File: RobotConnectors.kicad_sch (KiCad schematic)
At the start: 68 parts, among them J1 Conn_02x11_Top_Bottom, J10 Conn_01x05, J11 Conn_01x03_Male, J12 Conn_01x03_Male, J13 Conn_01x03_Male, J14 Conn_01x03_Male, J17 Conn_01x02, J18 Conn_01x02, J19 Conn_01x04, J2 Conn_02x04_Top_Bottom, J21 Conn_01x05, J27 Conn_01x03_Male, J28 Conn_01x03_Male, J29 Conn_01x03_Male, J3 Conn_01x02, J30 Conn_01x03_Male, J4 Conn_01x04, J5 Conn_01x04, J6 Conn_01x04, J7 Conn_01x04, J8 Conn_01x04, J9 Conn_01x04, U11 TXS0108EPW, U12 TXS0108EPW, U14 Fuse Holder, U15 Fuse Holder, U16 Fuse Holder, U17 Fuse Holder, U2 TPS2065CDBV, U28 Fuse 2A, U29 Fuse 2A

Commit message: Add Robot-Adapter and OEM plugs WIP
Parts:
- removed J11, J27, J28, J29, J30: Conn_01x03_Male, Connector_JST:JST_XH_B3B-XH-A_1x03_P2.50mm_Vertical, symbol Connector:Conn_01x03_Male
- removed J5, J6, J7, J8, J9: Conn_01x04, Connector_JST:JST_XH_B4B-XH-A_1x04_P2.50mm_Vertical, symbol Connector_Generic:Conn_01x04
- removed U11, U12: TXS0108EPW, Package_SO:TSSOP-20_4.4x6.5mm_P0.65mm, symbol Logic_LevelTranslator:TXS0108EPW
- added C62: 4.7uF, Capacitor_SMD:C_0805_2012Metric, symbol Device:C
- added C77: 100nF@50V, Capacitor_SMD:C_0402_1005Metric, symbol Device:C
- added J11: SA/SC Perimeter Plug, nlbn:ZX-HY2_0-9PZZ_C7429585, symbol Connector:Conn_01x09_Pin
- added J15: Hall0 (Stop2), Connector_JST:JST_XH_B3B-XH-A_1x03_P2.50mm_Vertical, symbol Connector:Conn_01x03_Male
- added J27: Rear Stop Switch 2, nlbn:HC-HY-2A_C2845460, symbol Connector:Conn_01x02_Pin
- added J40: Rear Stop Switch 1, nlbn:HC-HY-2A_C2845460, symbol Connector:Conn_01x02_Pin
- added J5: OEM CoverUI, nlbn:HDR-IDC-2_54-2X8P_C3406, symbol Connector_Generic:Conn_02x08_Odd_Even
- added J6: Conn_01x11_Socket, Connector_PinSocket_2.54mm:PinSocket_1x13_P2.54mm_Vertical, symbol Connector:Conn_01x13_Socket
- added J7: USS 1-5, Connector_PinSocket_2.54mm:PinSocket_1x12_P2.54mm_Vertical, symbol Connector:Conn_01x12_Socket
- added J8: Hall5 (Lift Left 2), Connector_JST:JST_XH_B3B-XH-A_1x03_P2.50mm_Vertical, symbol Connector:Conn_01x03_Male
- added J9: Hall4 (Lift Right 2), Connector_JST:JST_XH_B3B-XH-A_1x03_P2.50mm_Vertical, symbol Connector:Conn_01x03_Male
- added R28, R29, R30, R31, R32, R36, R37, R38, R39, R40, R42, R43, R60, R65: 10k, Resistor_SMD:R_0402_1005Metric, symbol Device:R
- added TP2: Hall6 (unused), TestPoint:TestPoint_Pad_D1.5mm, symbol Connector:TestPoint
- added U11, U12: SN74LVC07ADBR, nlbn:SN74LVC07ADBR_C2676799, symbol nlbn:SN74LVC07ADBR_C2676799
- added U47, U48: SN74LVC157ADR, PCM_JLCPCB:SOIC-16_3.9x9.9mm_P1.27mm, symbol 74xx:74LS157
- J12: value Conn_01x03_Male -> Hall3 (Lift Left)
- J13: value Conn_01x03_Male -> Hall2 (Lift Right)
- J14: value Conn_01x03_Male -> Hall1 (Stop1)
- R61, R62, R63, R64: now fitted
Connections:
- net 3.3V: now also C20.2, R48.1, R49.1, R50.1, C77.1, R28.1, R29.1, R60.1, R65.1, U11.14 (VCC), U12.14 (VCC), U47.16 (VCC), U48.16 (VCC); no longer R62.1
- net 5V: now also R62.1, C62.1, J15.1 (Pin_1), J5.9 (Pin_9), J6.1 (Pin_1), J7.1 (Pin_1), J8.1 (Pin_1), J9.1 (Pin_1), R30.1, R31.1, R32.1, R36.1, R37.1, R38.1, R39.1, R40.1, R42.1, R43.1; no longer C20.1, R48.1, R49.1, R50.1
- net GND: now also C20.1, C62.2, C77.2, J11.8 (Pin_8), J15.3 (Pin_3), J27.2 (Pin_2), J5.13 (Pin_13), J5.7 (Pin_7), J5.8 (Pin_8), J6.13 (Pin_13), J7.12 (Pin_12), J8.3 (Pin_3), J9.3 (Pin_3), U11.13 (6A), U11.7 (GND), U12.13 (6A), U12.7 (GND), U47.15 (E), U47.8 (GND), U48.15 (E), U48.2 (I0a), U48.3 (I1a), U48.8 (GND); no longer C20.2
- net HALL0: now also U47.12 (Zd); no longer R61.2
- net HALL0_5V: now also J15.2 (Pin_2), R40.2, U47.14 (I0d); no longer R51.2
- net HALL1: now also U47.9 (Zc); no longer R62.2
- net HALL1_5V: now also J14.2 (Pin_2), R39.2, U47.11 (I0c); no longer R50.2
- net HALL2: now also U47.7 (Zb); no longer R63.2
- net HALL2_5V: now also R38.2, U47.5 (I0b); no longer J14.2 (Pin_2), R49.2
- net HALL3: now also U47.4 (Za); no longer R64.2
- net HALL3_5V: now also R51.2, U47.2 (I0a); no longer R48.2
- net LED_RX: now also J5.3 (Pin_3)
- net LED_TX: now also J5.1 (Pin_1)
- net RAIN_SENSE: now also J5.11 (Pin_11)
- net USS1_ECHO: now also R28.2, U12.2 (1Y)
- net USS1_TRIGGER: now also U11.1 (1A)
- net USS2_ECHO: now also R29.2, U12.4 (2Y)
- net USS2_TRIGGER: now also U11.3 (2A)
- net USS3_ECHO: now also R48.2, U12.6 (3Y)
- net USS3_TRIGGER: now also U11.5 (3A)
- net USS4_ECHO: now also R50.2, U12.8 (4Y)
- net USS4_TRIGGER: now also U11.9 (4A)
- net USS5_ECHO: now also R49.2, U12.10 (5Y)
- net USS5_TRIGGER: now also U11.11 (5A)
- net USS_1_ECHO_5V: now also J7.11 (Pin_11), U12.1 (1A)
- net USS_1_TRIGGER_5V: now also J7.10 (Pin_10), R30.2, U11.2 (1Y)
- net USS_2_ECHO_5V: now also J7.9 (Pin_9), U12.3 (2A)
- net USS_2_TRIGGER_5V: now also J7.8 (Pin_8), R31.2, U11.4 (2Y)
- net USS_3_ECHO_5V: now also J7.7 (Pin_7), U12.5 (3A)
- net USS_3_TRIGGER_5V: now also J7.6 (Pin_6), R32.2, U11.6 (3Y)
- net USS_4_ECHO_5V: now also J7.5 (Pin_5), U12.9 (4A)
- net USS_4_TRIGGER_5V: now also J7.4 (Pin_4), R36.2, U11.8 (4Y)
- net USS_5_ECHO_5V: now also J7.3 (Pin_3), U12.11 (5A)
- net USS_5_TRIGGER_5V: now also J7.2 (Pin_2), R37.2, U11.10 (5Y)
- net RAIN: now reaches C15.1, D21.1 (K), J17.1 (Pin_1), R47.2
- net RAIN: now also J11.3 (Pin_3)
- new net: J27.1 (Pin_1), J40.2 (Pin_2)
- new net BTN_ANY: J5.2 (Pin_2)
- new net BTN_HOME_OEM: J5.5 (Pin_5), R64.2
- new net BTN_PLAY_OEM: J5.4 (Pin_4), R65.2
- new net HALL4: U48.12 (Zd)
- new net HALL4_5V: J9.2 (Pin_2), R43.2, U48.14 (I0d)
- new net HALL5: U48.9 (Zc)
- new net HALL5_5V: J8.2 (Pin_2), R42.2, U48.11 (I0c)
- new net HALL6: U48.7 (Zb)
- new net HALL6_5V: R62.2, TP2.1, U48.5 (I0b)
- new net HALL_SELECT_OEM: U47.1 (S), U48.1 (S)
- new net LLIFT2_LIFT_OEM: J5.16 (Pin_16), U48.10 (I1c)
- new net LLIFT_LBUMP_OEM: J5.12 (Pin_12), U47.3 (I1a)
- new net REAR_STOP_OEM: J40.1 (Pin_1), R63.2, U48.6 (I1b)
- new net RLIFT2_RBUMP_OEM: J5.15 (Pin_15), U48.13 (I1d)
- new net RLIFT_LIFTX_OEM: J5.10 (Pin_10), U47.6 (I1b)
- new net STOP1_OEM: J11.1 (Pin_1), J5.6 (Pin_6), R61.2, U47.10 (I1c)
- new net STOP2_OEM: J11.2 (Pin_2), J5.14 (Pin_14), R60.2, U47.13 (I1d)
- no-connect marks 5 -> 12
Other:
- note added: "Hall"
- note added: "USS"
- note added: "Validated with: C500B SA/SC 10BTN/12LED SA650 9BTN/11LED SAx Pro LCD NX100i"
- note removed: "Hall sensors (emergency etc)"
- moved on the sheet: C15, C17, C18, C19, C20, C54, C57, C60, C61, D21, D3, F4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

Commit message: Finished generic routing
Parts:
- removed TP2: Hall6 (unused), TestPoint:TestPoint_Pad_D1.5mm, symbol Connector:TestPoint
- J6: value Conn_01x11_Socket -> Conn_01x14_Socket; footprint Connector_PinSocket_2.54mm:PinSocket_1x13_P2.54mm_Vertical -> Connector_PinSocket_2.54mm:PinSocket_1x14_P2.54mm_Vertical; symbol Connector:Conn_01x13_Socket -> Connector:Conn_01x14_Socket
- U47, U48: footprint PCM_JLCPCB:SOIC-16_3.9x9.9mm_P1.27mm -> Package_SO:SOIC-16_3.9x9.9mm_P1.27mm
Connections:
- net BTN_HOME_OEM: now also J6.10 (Pin_10)
- net BTN_PLAY_OEM: now also J6.9 (Pin_9)
- net GND: now also J6.14 (Pin_14); no longer J6.13 (Pin_13)
- net HALL0_5V: now also J6.2 (Pin_2)
- net HALL1_5V: now also J6.3 (Pin_3)
- net HALL2_5V: now also J6.4 (Pin_4)
- net HALL3_5V: now also J6.5 (Pin_5)
- net HALL4_5V: now also J6.6 (Pin_6)
- net HALL5_5V: now also J6.7 (Pin_7)
- net HALL6_5V: now also J6.8 (Pin_8)
- net LED_RX: now also J6.12 (Pin_12)
- net LED_TX: now also J6.11 (Pin_11)
- net RAIN: now also J6.13 (Pin_13)
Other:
- moved on the sheet: C18, C62, J5, R64, R65

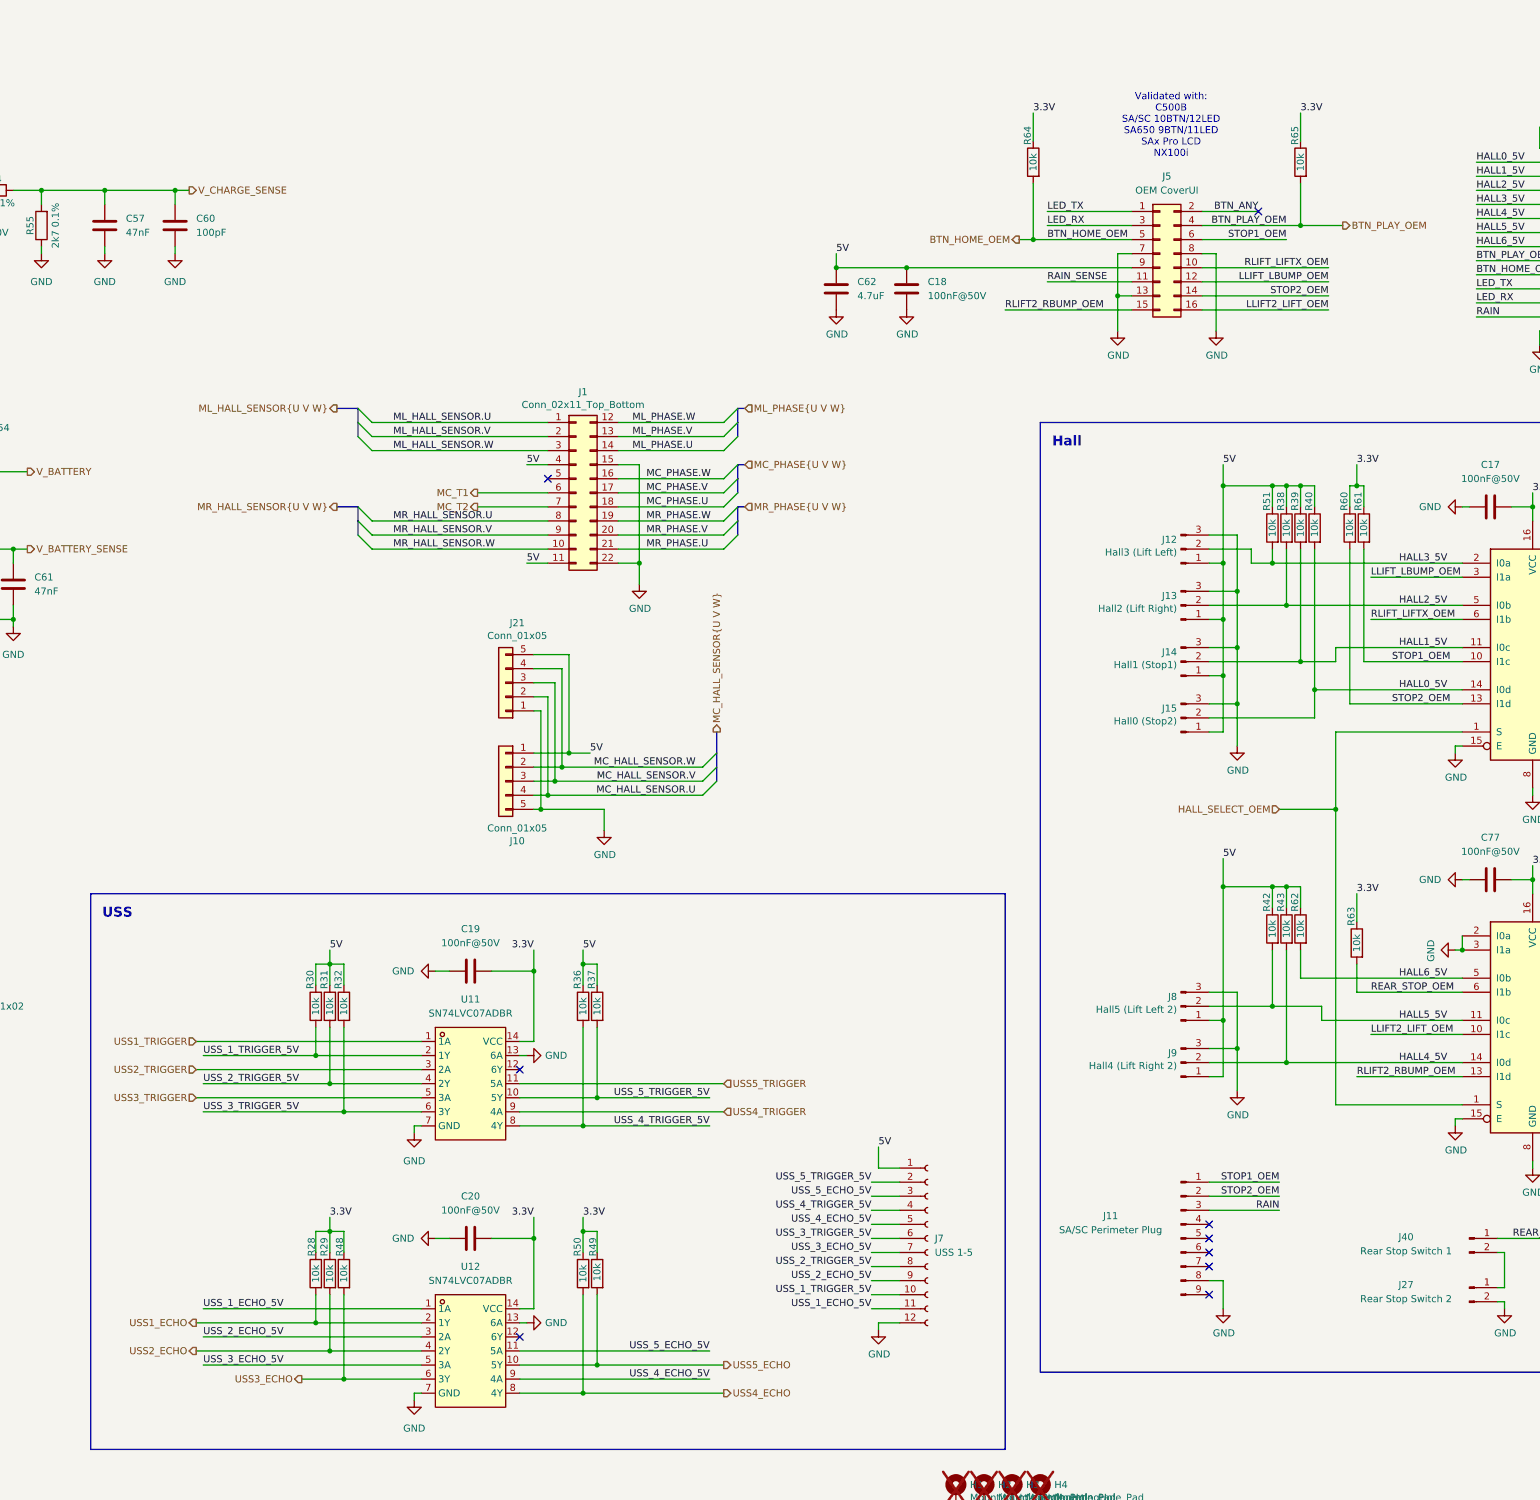
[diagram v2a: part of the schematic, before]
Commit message: Make OEM Buttons 5V tolerant
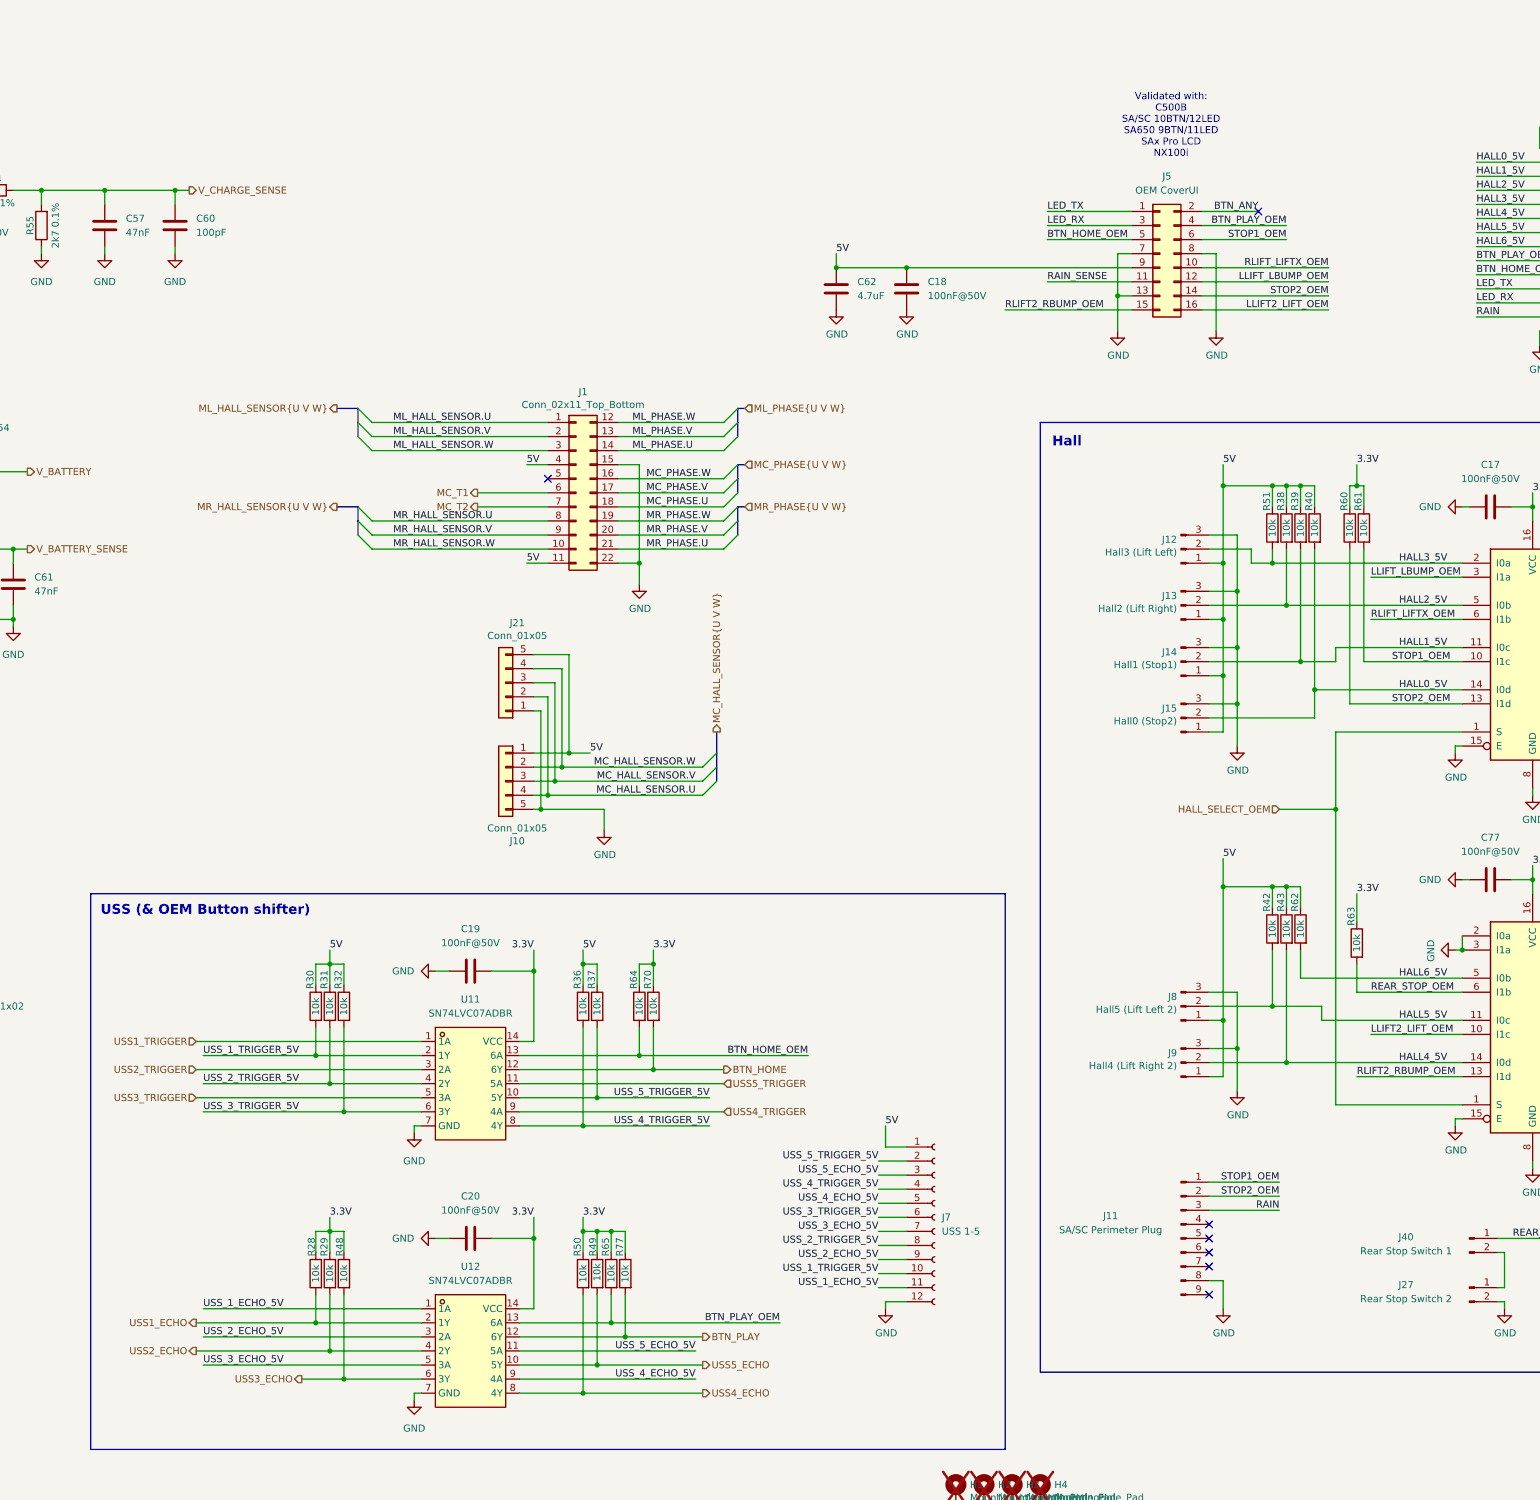
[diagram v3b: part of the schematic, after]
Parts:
- added R70, R77: 10k, Resistor_SMD:R_0402_1005Metric, symbol Device:R
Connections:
- net 3.3V: now also R70.1, R77.1
- net BTN_HOME_OEM: now also U11.13 (6A)
- net BTN_PLAY_OEM: now also U12.13 (6A)
- net GND: no longer U11.13 (6A), U12.13 (6A)
- net BTN_PLAY: now reaches U12.12 (6Y)
- net BTN_PLAY: now also R77.2
- net BTN_HOME: now reaches U11.12 (6Y)
- net BTN_HOME: now also R70.2
- no-connect marks 12 -> 10
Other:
- note added: "USS (& OEM Button shifter)"
- note removed: "USS"
- moved on the sheet: J7, R64, R65
